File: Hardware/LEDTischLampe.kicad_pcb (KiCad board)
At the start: 2 copper layers, 160 x 160 mm, 133 parts, among them IC1 RY8310, J1 Conn_01x02_Socket, J2 USB_C_Receptacle_USB2.0_14P, J3 Conn_02x03_Counter_Clockwise, M1 P-CHANNEL-MOSFET, SW1 Reset, SW2 User, U1 ESP32-C3-WROOM-02, U2 SY7200AABC, U3 SY7200AABC, U4 SY7200AABC, U5 SY7200AABC, U6 SY7200AABC

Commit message: edit layout
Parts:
- added H1: MountingHole, MountingHole:MountingHole_3.2mm_M3, F.Cu at (124.6, 94.0)
- added H2: MountingHole, MountingHole:MountingHole_3.2mm_M3, F.Cu at (144.6, 94.0)
- moved C17 107.8 mm to (166.0, 56.2), turned to 90 degrees
- moved R9 104.2 mm to (163.3, 55.2), turned to 90 degrees
- moved C10 102.6 mm to (161.0, 49.7), turned to 0 degrees
- moved C3 100.5 mm to (160.0, 52.0), turned to 0 degrees
- moved U3 100.4 mm to (160.5, 54.8), turned to -90 degrees
- moved D5 99.3 mm to (160.2, 58.8), turned to 180 degrees
- moved L8 96.0 mm to (157.3, 54.9), turned to 90 degrees
- moved C7 62.5 mm to (145.8, 76.0)
- moved R13 54.2 mm to (146.8, 67.1), turned to -90 degrees
- moved C8 53.8 mm to (145.7, 67.1)
- moved R14 32.2 mm to (179.9, 36.7), turned to -123.75 degrees
- moved C4 31.6 mm to (118.4, 108.3)
- moved IC1 31.6 mm to (118.4, 110.7)
- moved L1 31.6 mm to (121.3, 107.7)
- moved C1 31.6 mm to (121.0, 112.4)
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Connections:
- C8 pad 1: UserButton -> IO9
- R13 pad 2: UserButton -> IO9
- SW2 pad 2: UserButton -> IO9
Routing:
- net +3V3: track 0.00 -> 33.1 mm
- net EN: track 0.00 -> 20.2 mm, vias 0 -> 2
- net IO9: track 0.00 -> 14.8 mm
- net TX: track 0.00 -> 12.7 mm
- net RX: track 0.00 -> 10.0 mm
- net GND: track 31.6 -> 39.8 mm, vias 31 -> 41
- net DP: track 2.93 -> 10.1 mm, vias 0 -> 1
- net Net-(J2-CC1): track 1.54 -> 6.92 mm
- net /LedsOben/LedTreiber2/LEDN: track 6.92 -> 2.00 mm
- net /LedsOben/LedTreiber3/LEDN: track 6.92 -> 2.00 mm
- net Net-(J2-CC2): track 1.59 -> 6.42 mm
- net VCC: track 15.0 -> 17.8 mm
- net Net-(D34-A): track 0.00 -> 2.57 mm
- net Net-(D3-A): track 0.00 -> 1.09 mm
- net Net-(D2-A): track 0.00 -> 1.09 mm
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- added copper zone on B.Cu, net /LedsOben/LedTreiber2/LEDP
- added copper zone on F.Cu, net Net-(J1-Pin_1)
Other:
- outline, holes or cut-outs redrawn

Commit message: a bit more layouting
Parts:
- moved R12 51.1 mm to (145.8, 77.5), turned to 90 degrees
- moved D24 33.4 mm to (171.6, 55.1), turned to 90 degrees
- moved C14 19.0 mm to (179.9, 119.0)
- moved U2 19.0 mm to (177.2, 119.4)
- moved C13 19.0 mm to (182.2, 120.0)
- moved C15 19.0 mm to (175.7, 124.9)
- moved D26 19.0 mm to (173.1, 119.2)
- moved L11 19.0 mm to (177.1, 116.3)
- moved R16 19.0 mm to (176.7, 122.2)
- moved D5 16.3 mm to (146.4, 50.3)
- moved U3 16.3 mm to (146.6, 46.2)
- moved C3 16.3 mm to (146.1, 43.5)
- moved L8 16.3 mm to (143.4, 46.3)
- moved C10 16.3 mm to (147.1, 41.2)
- moved C17 16.3 mm to (152.1, 47.7)
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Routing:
- net /LedsUnten/LedTreiber4/LEDP: track 13.2 -> 55.5 mm, vias 2 -> 6
- net /LedsOben/LedTreiber1/LEDP: track 12.5 -> 51.8 mm, vias 2 -> 4
- net /LedsOben/LedTreiber1/LEDN: track 7.96 -> 26.1 mm, vias 0 -> 2
- net /LedsOben/LedTreiber5/LEDP: track 12.5 -> 27.7 mm, vias 2 -> 4
- net /LedsOben/LedTreiber5/LEDN: track 6.92 -> 19.7 mm
- net /LedsUnten/LedTreiber4/LEDN: track 6.92 -> 19.2 mm, vias 0 -> 2
- net Net-(D24-A): track 0.00 -> 11.6 mm, vias 0 -> 2
- net /LedsOben/LedTreiber2/LEDN: track 2.00 -> 13.3 mm
- net /LedsOben/LedTreiber3/LEDP: track 12.5 -> 23.1 mm, vias 2 -> 4
- net /LedsOben/LedTreiber2/LEDP: track 12.5 -> 21.1 mm, vias 8 -> 11
- net Net-(D4-RA): track 0.00 -> 2.93 mm
- net Net-(D4-BA): track 0.00 -> 2.81 mm
- net Net-(LED1-A): track 0.00 -> 2.80 mm
- net Net-(D9-BA): track 0.00 -> 2.53 mm
- net Net-(D9-GA): track 0.00 -> 2.51 mm
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- added copper zone on B.Cu, net GND

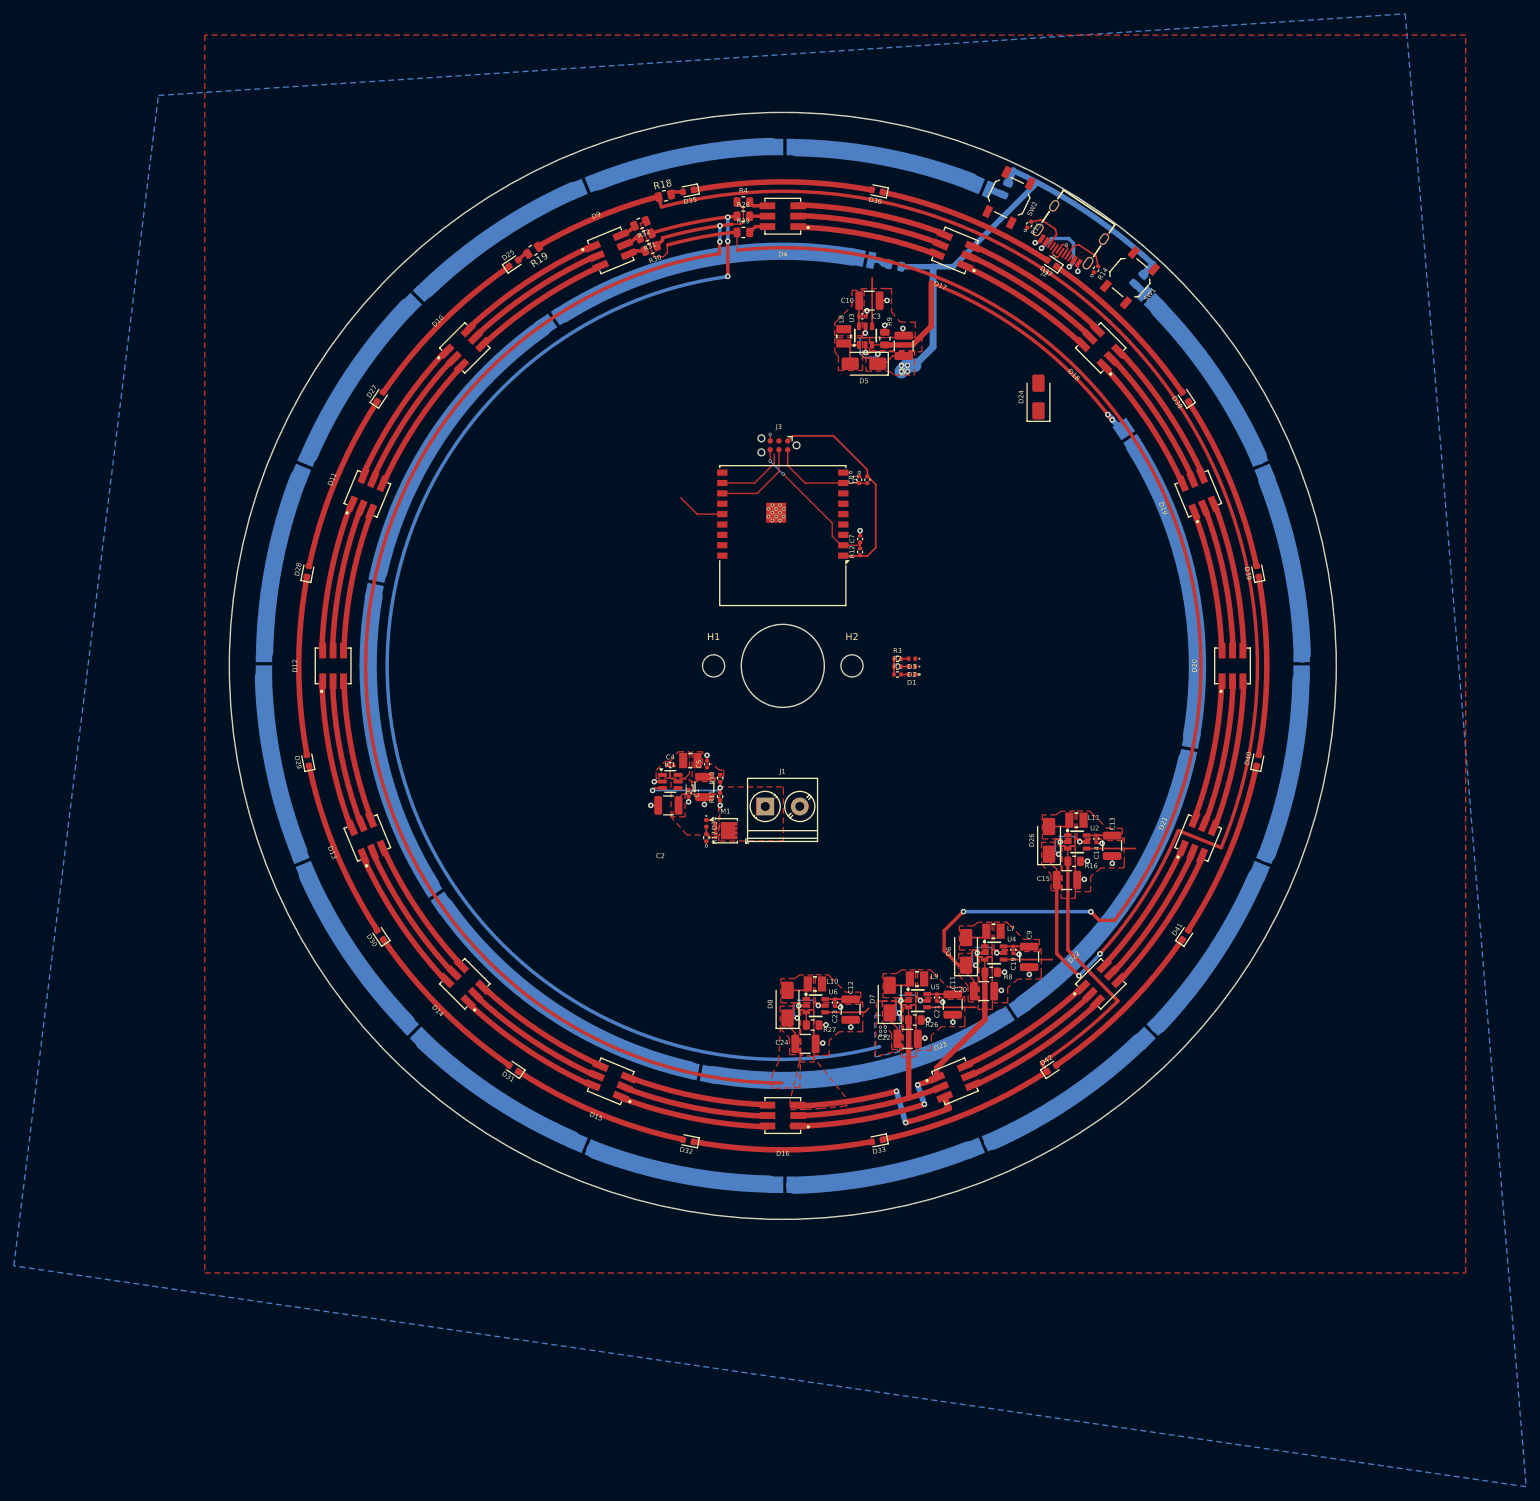
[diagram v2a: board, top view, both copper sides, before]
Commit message: finished preliminary routing
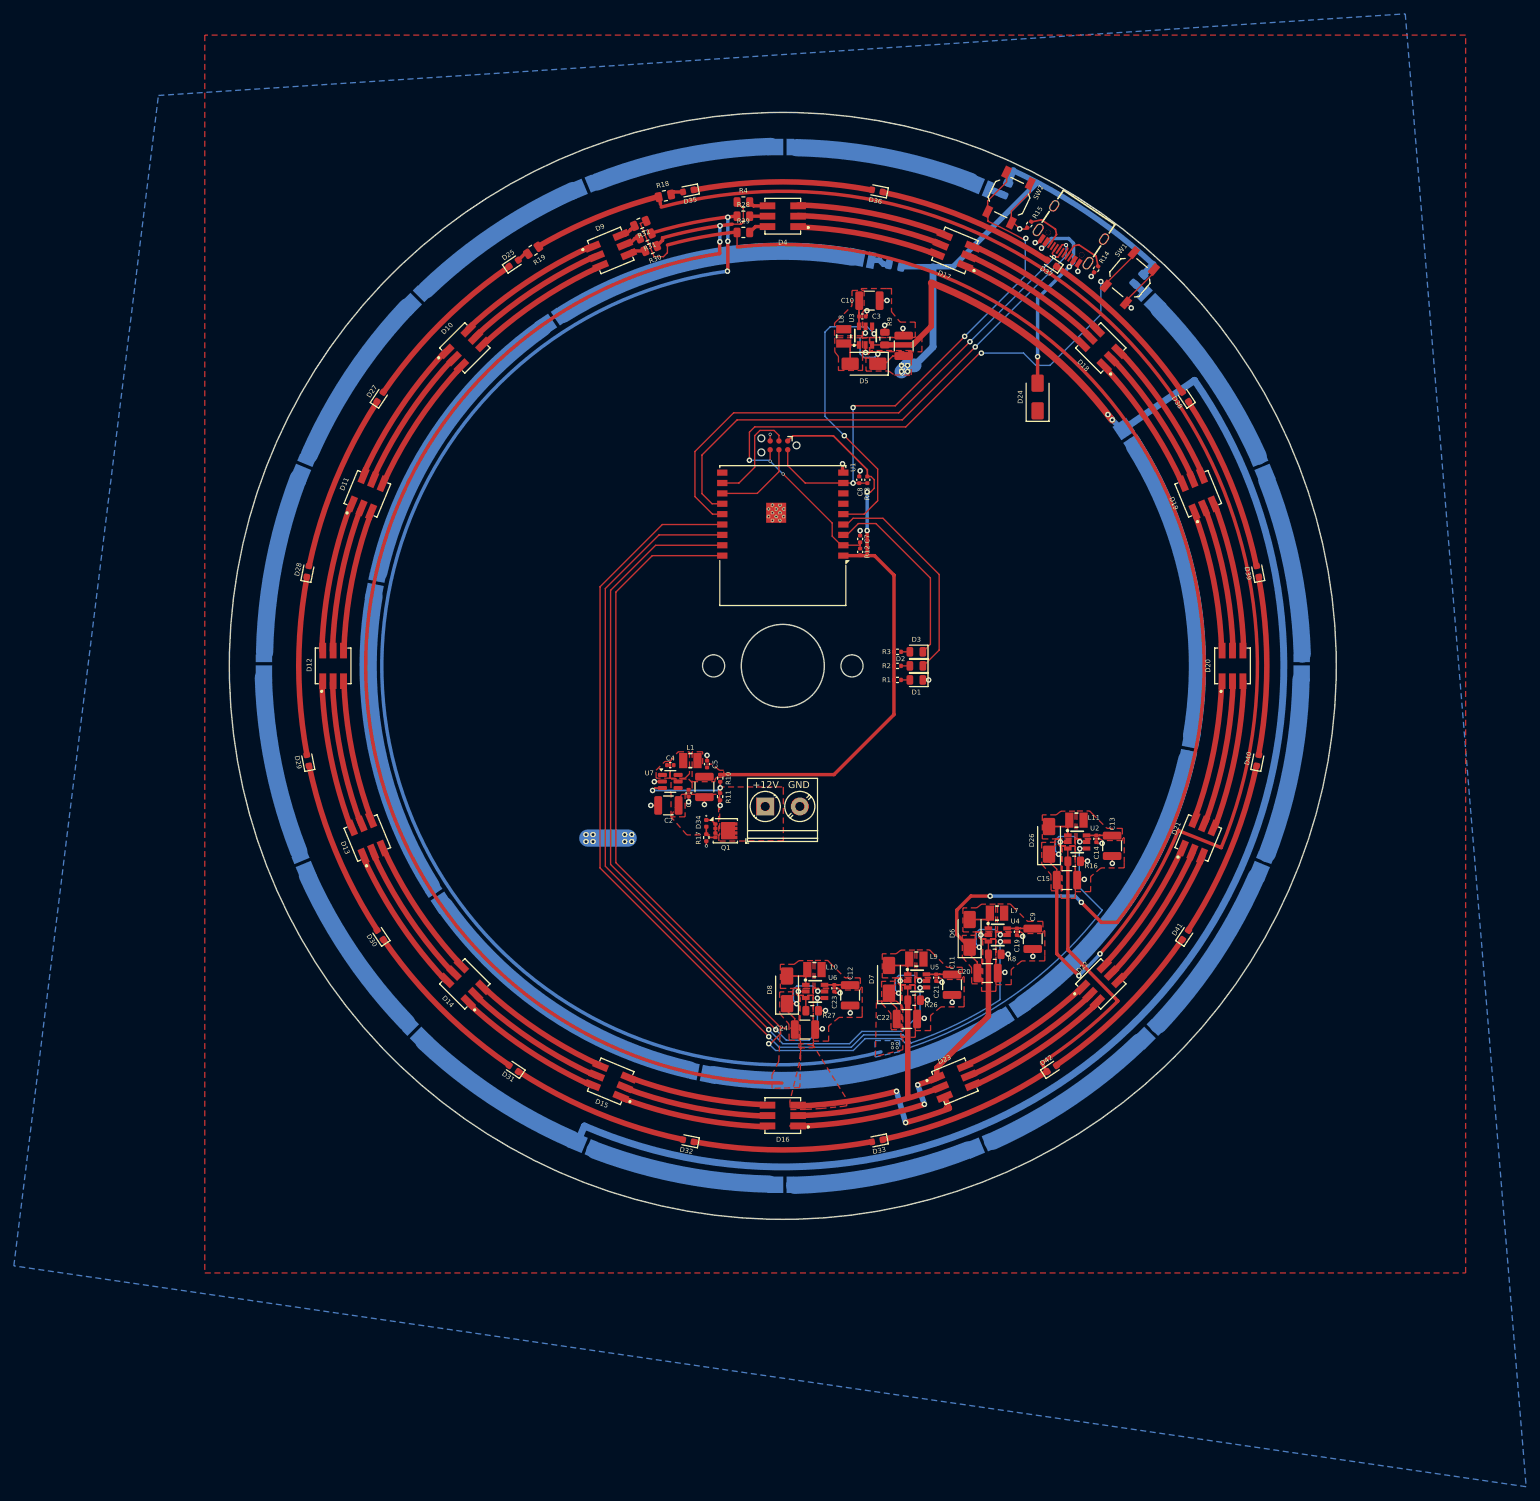
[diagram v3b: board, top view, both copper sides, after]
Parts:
- D1: value LED -> Power; footprint LED_SMD:LED_0402_1005Metric -> LED_SMD:LED_0805_2012Metric
- D2: value LED -> Status0; footprint LED_SMD:LED_0402_1005Metric -> LED_SMD:LED_0805_2012Metric
- D3: value LED -> Status1; footprint LED_SMD:LED_0402_1005Metric -> LED_SMD:LED_0805_2012Metric
- R1, R2, R3: value 1k -> 4k7
- moved C22 2.87 mm to (152.6, 145.0)
- moved D7 2.87 mm to (150.0, 139.3)
- moved C11 2.87 mm to (159.1, 140.1)
- moved C21 2.87 mm to (156.8, 139.1)
- moved L9 2.87 mm to (153.9, 136.4)
- moved U5 2.87 mm to (154.0, 139.5)
- moved R26 2.87 mm to (153.6, 142.3)
- moved C19 2.66 mm to (168.5, 132.4)
- moved D6 2.66 mm to (161.6, 132.6)
- moved R8 2.66 mm to (165.3, 135.7)
- moved U4 2.66 mm to (165.7, 132.9)
- moved C9 2.66 mm to (170.7, 133.4)
- moved L7 2.66 mm to (165.6, 129.7)
- moved C20 2.66 mm to (164.2, 138.4)
- moved C24 2.07 mm to (137.8, 146.5)
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- renumbered M1 to Q1, IC1 to U7
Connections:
- C10 pad 1: +12V -> VCC
- C3 pad 1: +12V -> VCC
- L8 pad 1: +12V -> VCC
- U1 pad 18: unconnected-(U1-IO0-Pad18) -> ADim
- U1 pad 3: WhiteDim -> StateLed01
- U1 pad 4: unconnected-(U1-IO5-Pad4) -> StateLed00
- U1 pad 5: unconnected-(U1-IO6-Pad5) -> WhiteDim
- U3 pad 6: +12V -> VCC
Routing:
- net RDim: track 7.04 -> 128.3 mm, vias 0 -> 2
- net ADim: track 7.02 -> 126.8 mm, vias 0 -> 2
- net GDim: track 7.02 -> 122.8 mm, vias 0 -> 2
- net BDim: track 6.56 -> 105.3 mm, vias 0 -> 2
- net EN: track 21.0 -> 99.7 mm, vias 2 -> 5
- net DN: track 3.08 -> 78.3 mm, vias 1 -> 2
- net DP: track 10.1 -> 78.2 mm, vias 1 -> 2
- net IO9: track 14.8 -> 72.3 mm, vias 0 -> 4
- net +3V3: track 33.1 -> 85.1 mm, vias 0 -> 2
- net WhiteDim: track 7.02 -> 42.4 mm, vias 0 -> 2
- net StateLed00: track 0.00 -> 32.0 mm
- net StateLed01: track 0.00 -> 27.6 mm
- net Net-(D24-A): track 11.6 -> 30.3 mm, vias 2 -> 3
- net GND: track 39.9 -> 57.5 mm, vias 41 -> 42
- net VCC: track 18.2 -> 27.4 mm, vias 0 -> 8
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- removed copper zone on F.Cu, net +12V
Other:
- board text added: "+12V GND"
- board text added: "GND +12V"

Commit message: assign most LCSC numbers
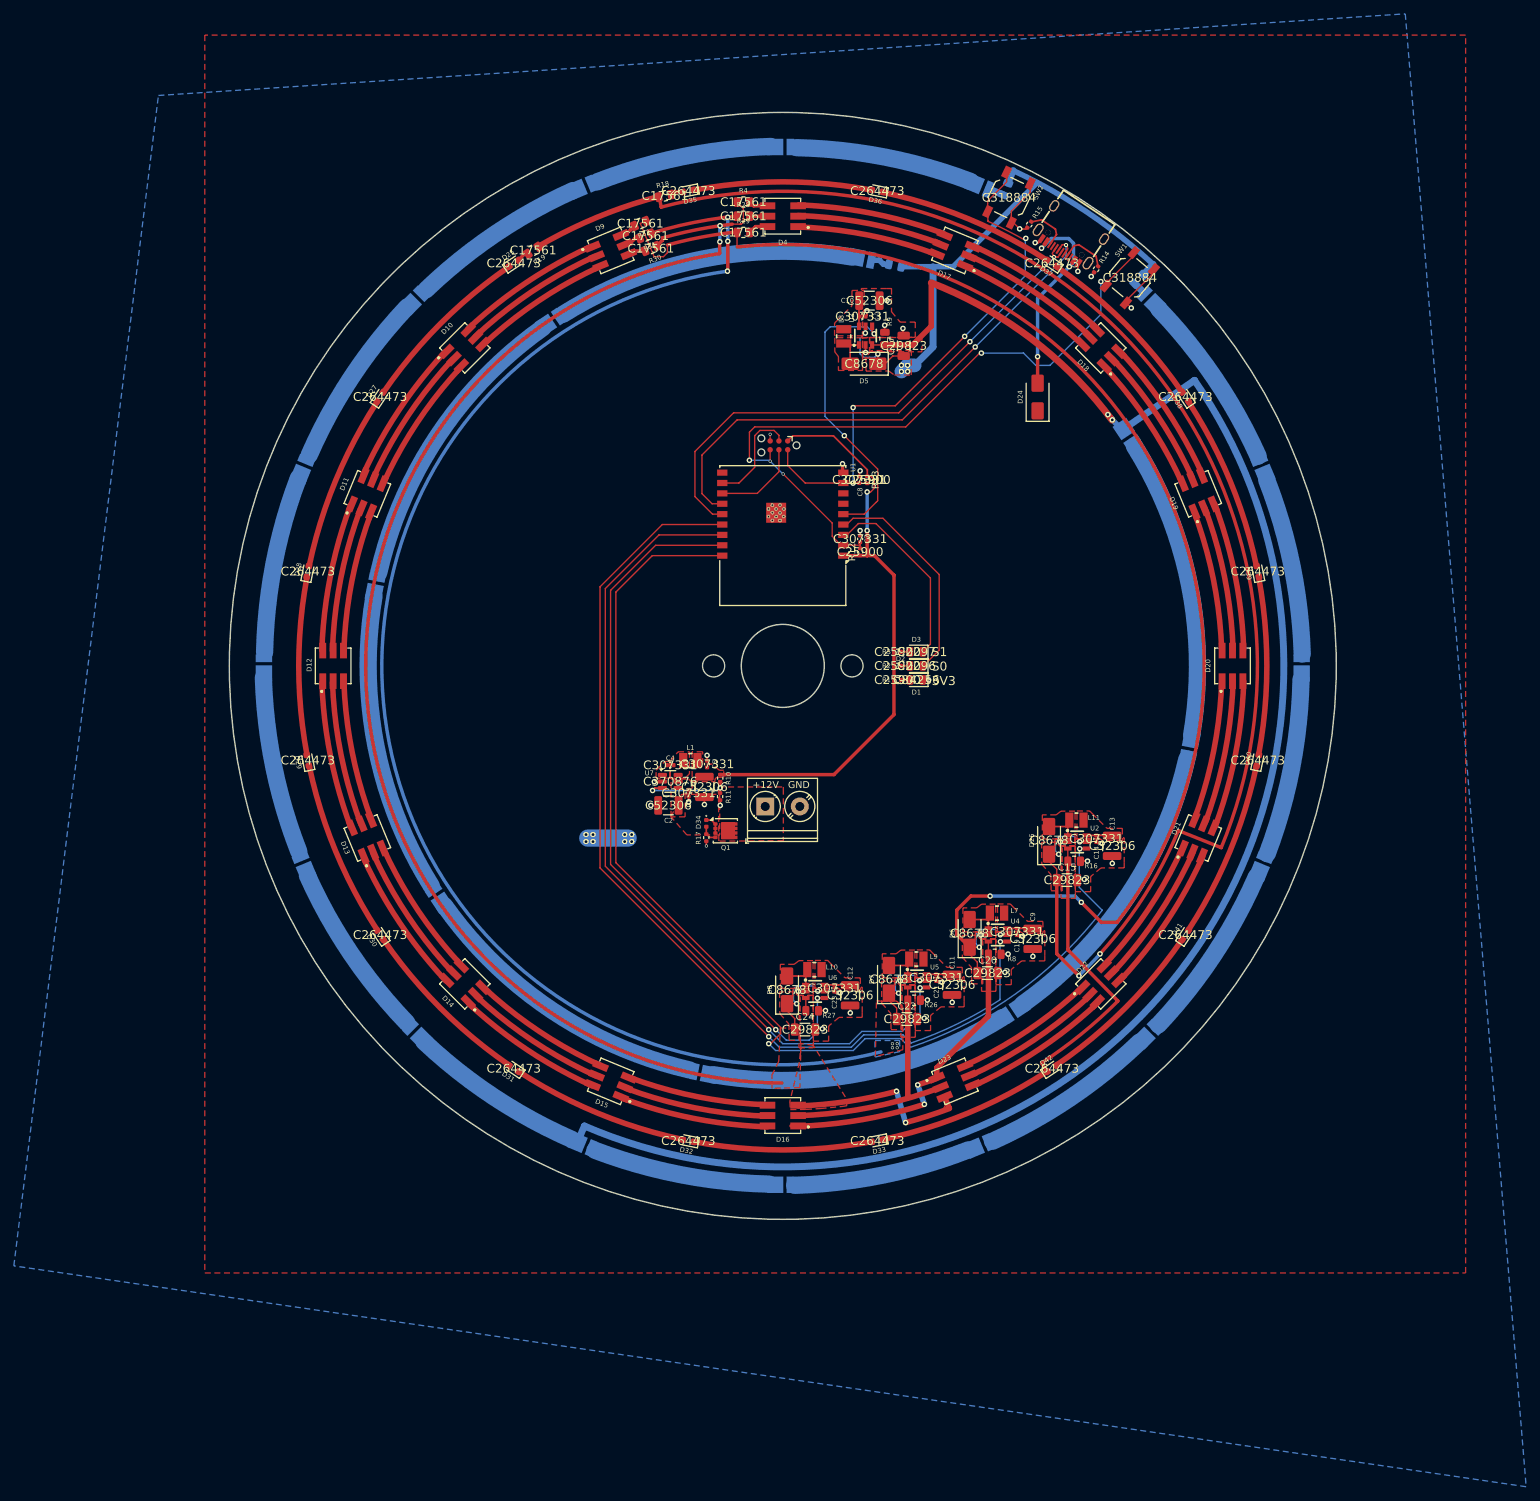
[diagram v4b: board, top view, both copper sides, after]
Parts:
- C15, C17, C20, C22, C24: footprint Capacitor_SMD:C_1210_3225Metric -> Capacitor_SMD:C_1206_3216Metric
- D24, D26, D5, D6, D7, D8: value D -> SS34
- R10: value 31,25k -> 47k
- R11: value 10k -> 15k
- R12, R13: footprint Capacitor_SMD:C_0402_1005Metric -> Resistor_SMD:R_0402_1005Metric
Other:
- board text added: "S1 S0 3V3"
